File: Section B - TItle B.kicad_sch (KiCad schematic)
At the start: 25 parts, among them J5 JST_SHBM04B-SRSS-TB, J6 Conn_02x07_Odd_Even, J7 THD-20-R, J9 Micro_SD_Card_Det, SW1 Right angle Tact button, U3 74LVC1G07SE-7, U6 RT9742GGJ5

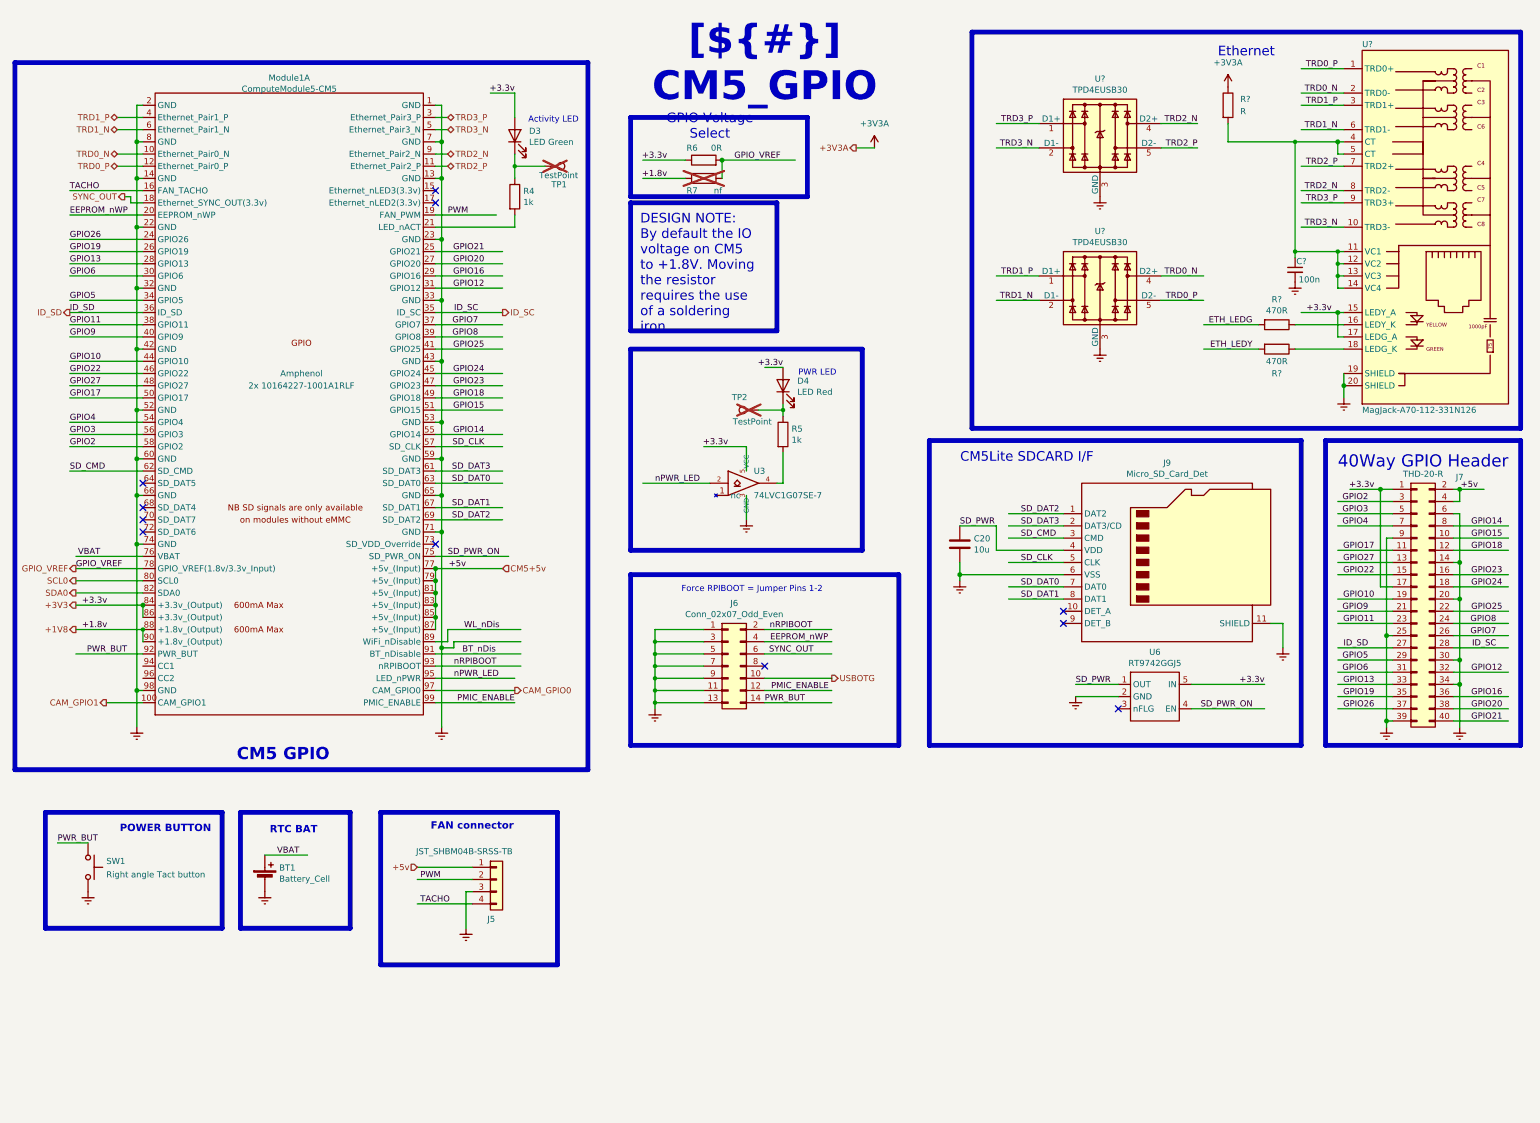
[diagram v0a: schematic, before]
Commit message: Sheets neatened
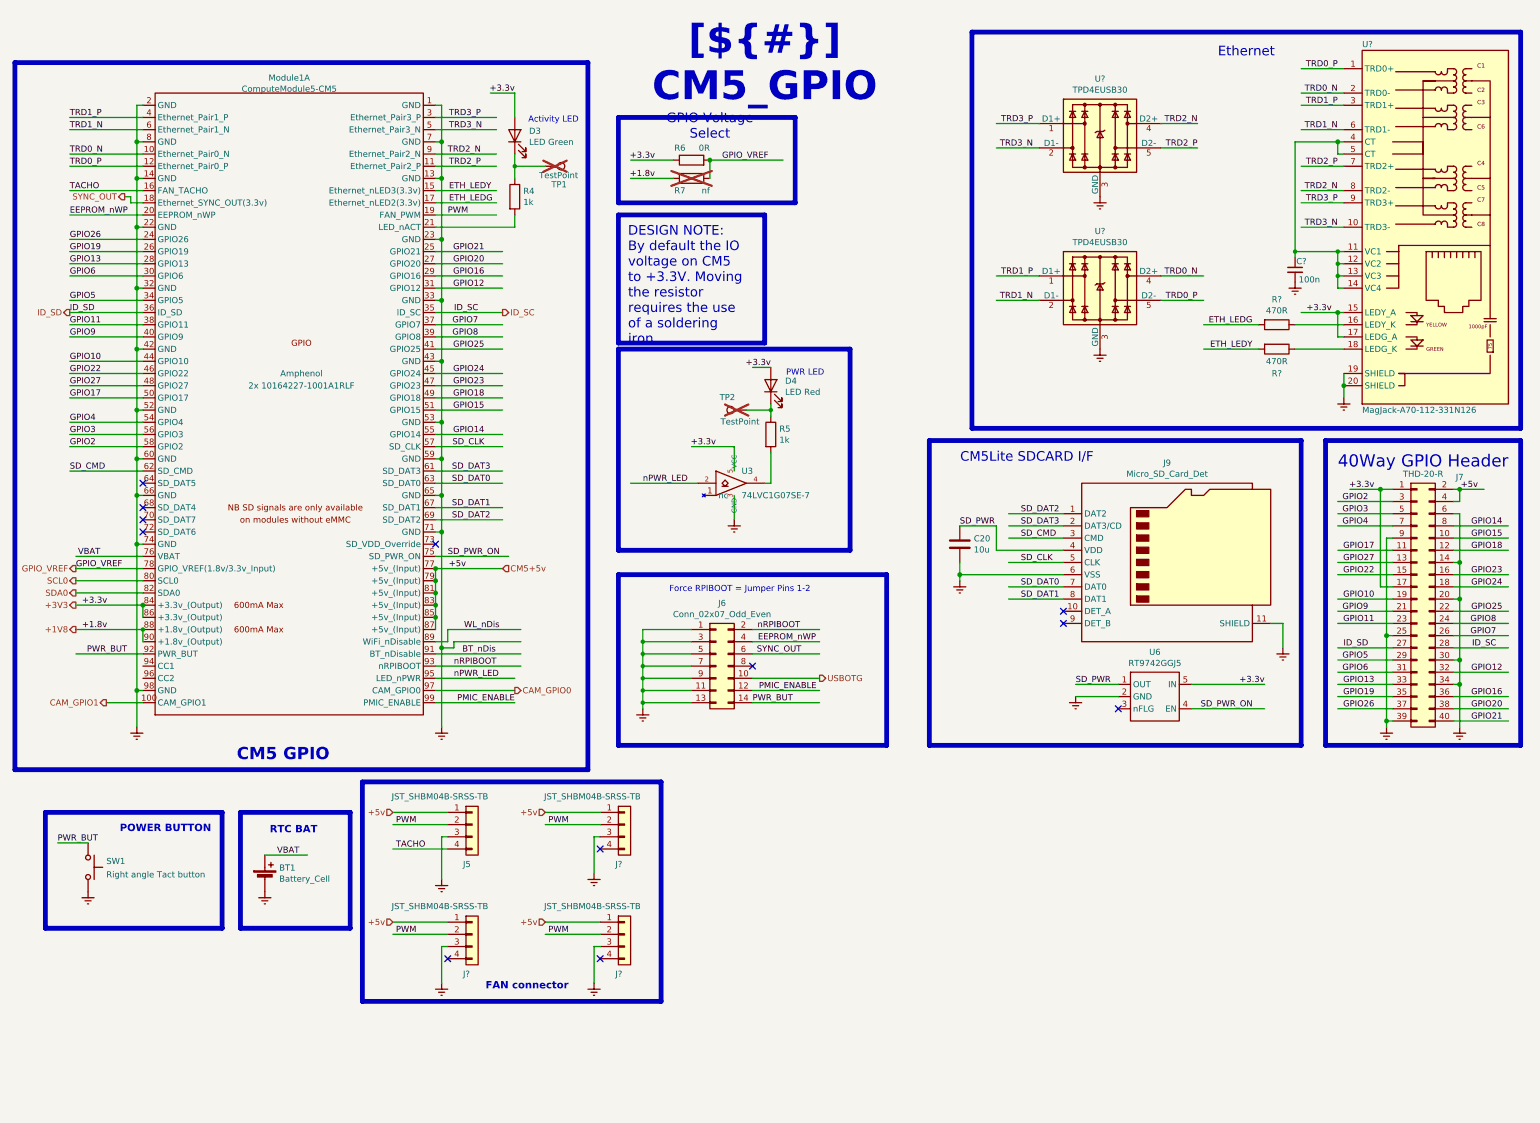
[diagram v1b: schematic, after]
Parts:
- removed R?: R, symbol Device:R
- added J? (x3): JST_SHBM04B-SRSS-TB, Connector_JST:JST_SH_BM04B-SRSS-TB_1x04-1MP_P1.00mm_Vertical, symbol Connector_Generic:Conn_01x04
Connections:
- net +5v: now also J?.1 (Pin_1), J?.1 (Pin_1), J?.1 (Pin_1)
- net ETH_LEDG: now also Module1.17 (Ethernet_nLED2(3.3v))
- net ETH_LEDY: now also Module1.15 (Ethernet_nLED3(3.3v))
- net PWM: now also J?.2 (Pin_2), J?.2 (Pin_2), J?.2 (Pin_2)
- no-connect marks 11 -> 12
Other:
- moved on the sheet: D4, J5, J6, R5, R6, R7, TP2, U3

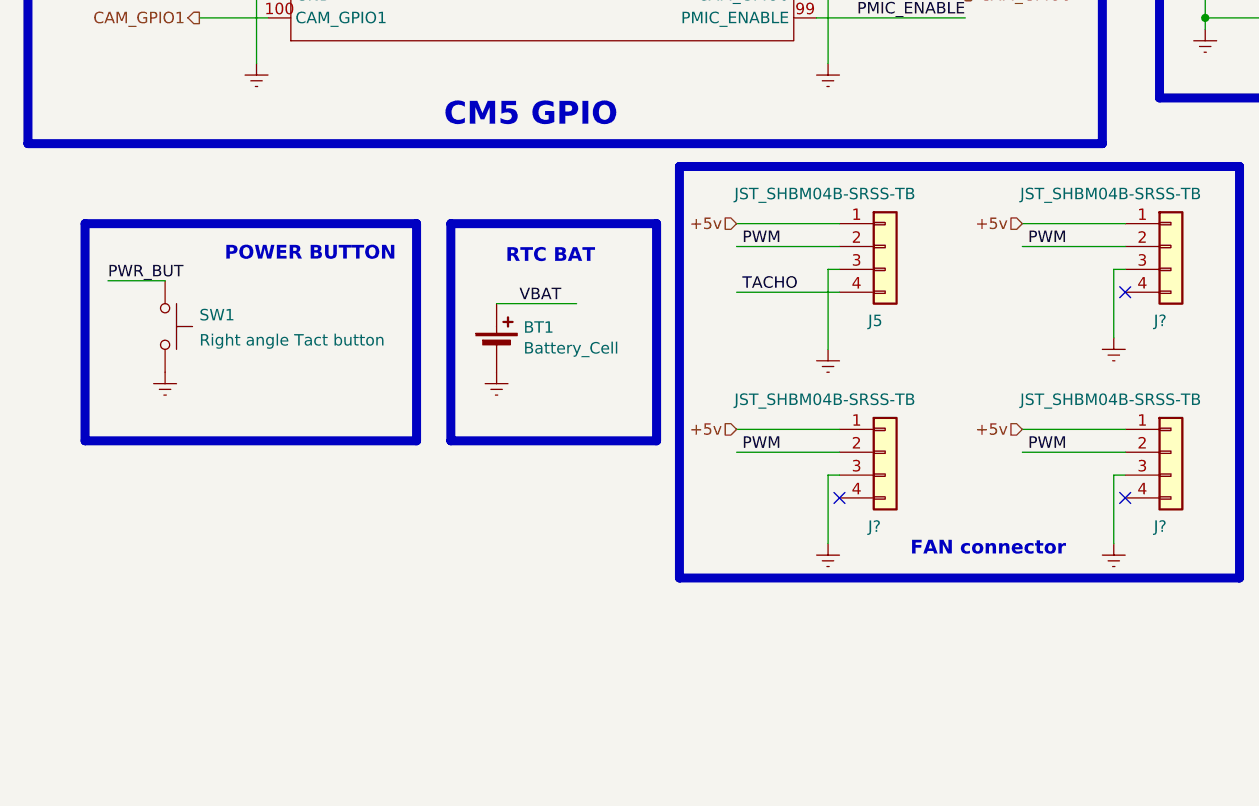
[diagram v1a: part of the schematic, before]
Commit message: More Fans
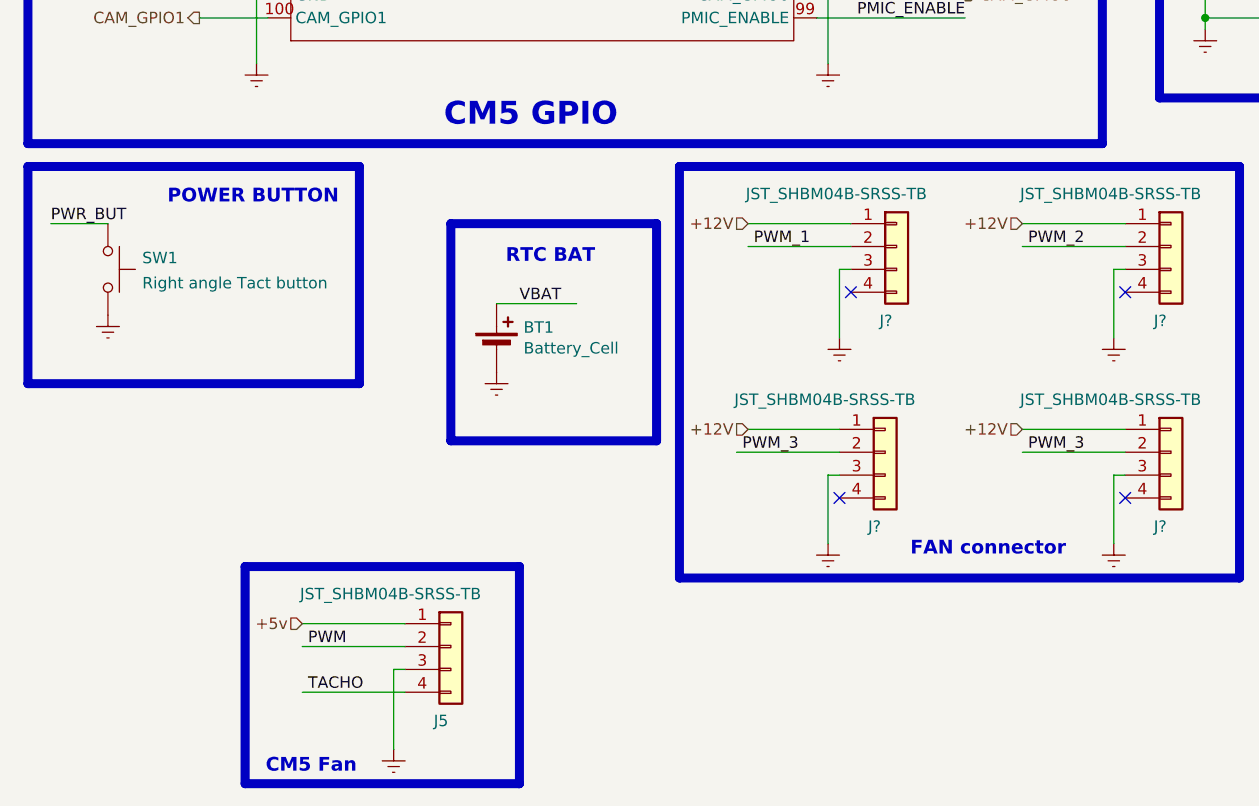
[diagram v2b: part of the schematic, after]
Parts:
- added J?: JST_SHBM04B-SRSS-TB, Connector_JST:JST_SH_BM04B-SRSS-TB_1x04-1MP_P1.00mm_Vertical, symbol Connector_Generic:Conn_01x04
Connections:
- net +5v: no longer J?.1 (Pin_1), J?.1 (Pin_1), J?.1 (Pin_1)
- net PWM: no longer J?.2 (Pin_2), J?.2 (Pin_2), J?.2 (Pin_2)
- new net +12V: J?.1 (Pin_1), J?.1 (Pin_1), J?.1 (Pin_1), J?.1 (Pin_1)
- new net PWM_1: J?.2 (Pin_2)
- new net PWM_2: J?.2 (Pin_2)
- new net PWM_3: J?.2 (Pin_2), J?.2 (Pin_2)
- no-connect marks 12 -> 13
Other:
- note added: "CM5 Fan"
- moved on the sheet: J5, J?, SW1
